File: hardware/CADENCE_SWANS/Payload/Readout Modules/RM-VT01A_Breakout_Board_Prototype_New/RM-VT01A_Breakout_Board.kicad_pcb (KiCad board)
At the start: 4 copper layers, 30.3 x 30.3 mm, 8 parts, among them J1 DE9_Pins

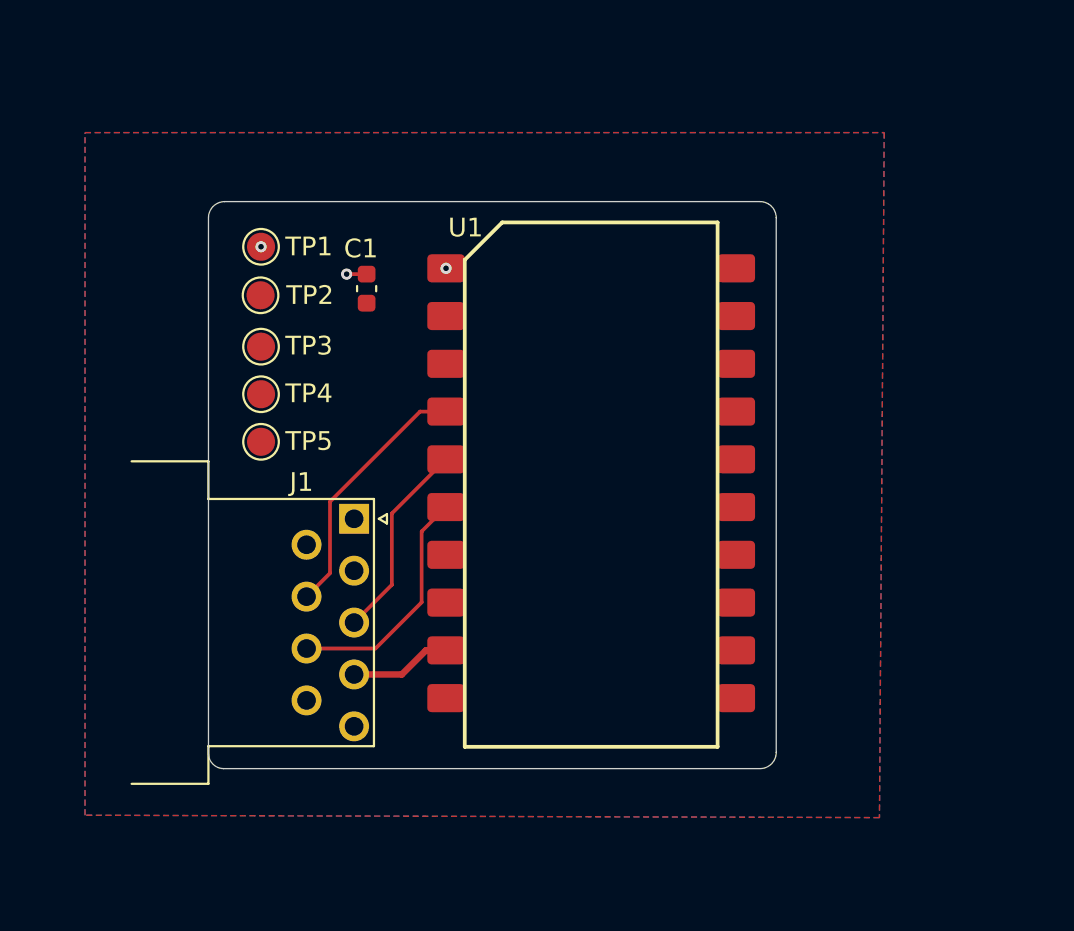
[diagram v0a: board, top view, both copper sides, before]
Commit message: Mounting Holes Included
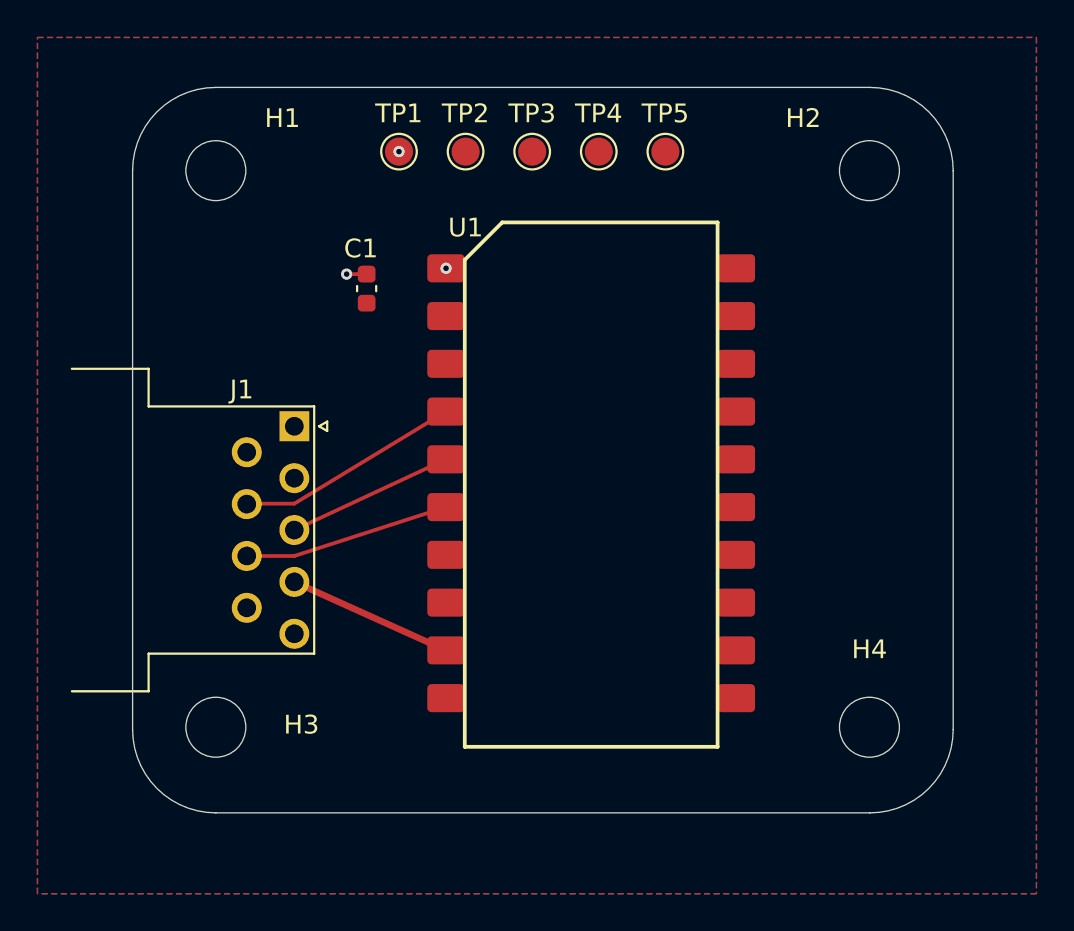
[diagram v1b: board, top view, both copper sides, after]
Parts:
- added H1: MountingHole, MountingHole:MountingHole_3.2mm_M3, F.Cu at (121.3, 68.1)
- added H2: MountingHole, MountingHole:MountingHole_3.2mm_M3, F.Cu at (156.2, 68.1)
- added H3: MountingHole, MountingHole:MountingHole_3.2mm_M3, F.Cu at (121.3, 97.8)
- added H4: MountingHole, MountingHole:MountingHole_3.2mm_M3, F.Cu at (156.2, 97.8)
- moved TP5 26.6 mm to (145.3, 67.1)
- moved TP4 22.2 mm to (141.7, 67.1)
- moved TP3 17.8 mm to (138.2, 67.1)
- moved TP2 13.4 mm to (134.6, 67.1)
- moved TP1 8.95 mm to (131.1, 67.1)
- moved J1 5.88 mm to (125.5, 81.7)
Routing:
- net CONN_COAXIAL: track 5.44 -> 8.89 mm
- net CTRL_EN: track 10.7 -> 8.94 mm
- net CTRL_R2: track 13.8 -> 12.0 mm
- net CTRL_R1: track 12.8 -> 11.0 mm
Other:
- board size 30.3 x 30.3 mm -> 43.8 x 38.7 mm

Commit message: Preliminary Update Payload
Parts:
- J1: footprint Connector_Dsub:DSUB-9_Pins_Horizontal_P2.77x2.54mm_EdgePinOffset9.40mm -> Imports:NORCOMP_380-009-213L001
- moved J1 2.47 mm to (124.4, 84.0), turned to 90 degrees
- renumbered TP4 to EN, TP2 to GND, TP5 to R1, TP3 to R2, TP1 to VDD
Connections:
- EN pad 1: unconnected-(TP4-Pad1) -> CTRL_EN
- R1 pad 1: unconnected-(TP5-Pad1) -> CTRL_R1
- R2 pad 1: unconnected-(TP3-Pad1) -> CTRL_R2
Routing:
- net CTRL_EN: track 8.94 -> 54.3 mm
- net CTRL_R1: track 11.0 -> 33.0 mm
- net CTRL_R2: track 12.0 -> 25.4 mm
- net CONN_COAXIAL: track 8.89 -> 15.8 mm
- net VDD: track 1.07 -> 4.59 mm, vias 3 -> 2
- net GND: vias 0 -> 3
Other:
- board text added: "Payload Instrument Board"
- board text removed: "Instrument Board"

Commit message: Revised Instrument Boards
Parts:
- removed the EN at (141.7, 67.1)
- removed the GND at (134.6, 67.1)
- removed the VDD at (131.1, 67.1)
- added EN: TestPoint, TestPoint:TestPoint_Loop_D2.60mm_Drill1.6mm_Beaded, F.Cu at (144.0, 66.3)
- added G***: LOGO, LOGO, B.Cu at (138.6, 92.5)
- added GND: TestPoint, TestPoint:TestPoint_Loop_D2.60mm_Drill1.6mm_Beaded, F.Cu at (134.6, 66.3)
- added VDD: TestPoint, TestPoint:TestPoint_Loop_D2.60mm_Drill1.6mm_Beaded, F.Cu at (129.9, 66.3)
- H1, H2, H3, H4: footprint MountingHole:MountingHole_3.2mm_M3 -> MountingHole:MountingHole_3.2mm_M3_ISO14580_Pad
- J1: footprint Imports:NORCOMP_380-009-213L001 -> Imports:CONN_381-009_NRC
- R1, R2: footprint TestPoint:TestPoint_Pad_D1.5mm -> TestPoint:TestPoint_Loop_D2.60mm_Drill1.6mm_Beaded
- moved J1 6.69 mm to (117.7, 83.8)
- moved R1 3.51 mm to (148.7, 66.3)
- moved R2 1.37 mm to (139.3, 66.3)
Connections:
- J1 pad 1: VDD -> CTRL_R2
- J1 pad 4: CONN_COAXIAL -> CTRL_R1
- J1 pad 5: GND -> CONN_COAXIAL
- J1 pad 6: unconnected-(J1-Pad6) -> VDD
- J1 pad 7: CTRL_R2 -> unconnected-(J1-Pad7)
- J1 pad 8: CTRL_R1 -> unconnected-(J1-Pad8)
- J1 pad 9: unconnected-(J1-Pad9) -> GND
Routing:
- net CTRL_EN: track 54.3 -> 27.9 mm
- net CONN_COAXIAL: track 15.8 -> 9.91 mm
- net CTRL_R2: track 25.4 -> 23.4 mm
- net VDD: track 4.59 -> 5.52 mm, vias 2 -> 1
- net GND: vias 3 -> 13
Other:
- board text added: "0.3493mm 50Ω"
- board text added: "Angelo Duenas Pragun Bethapudi"

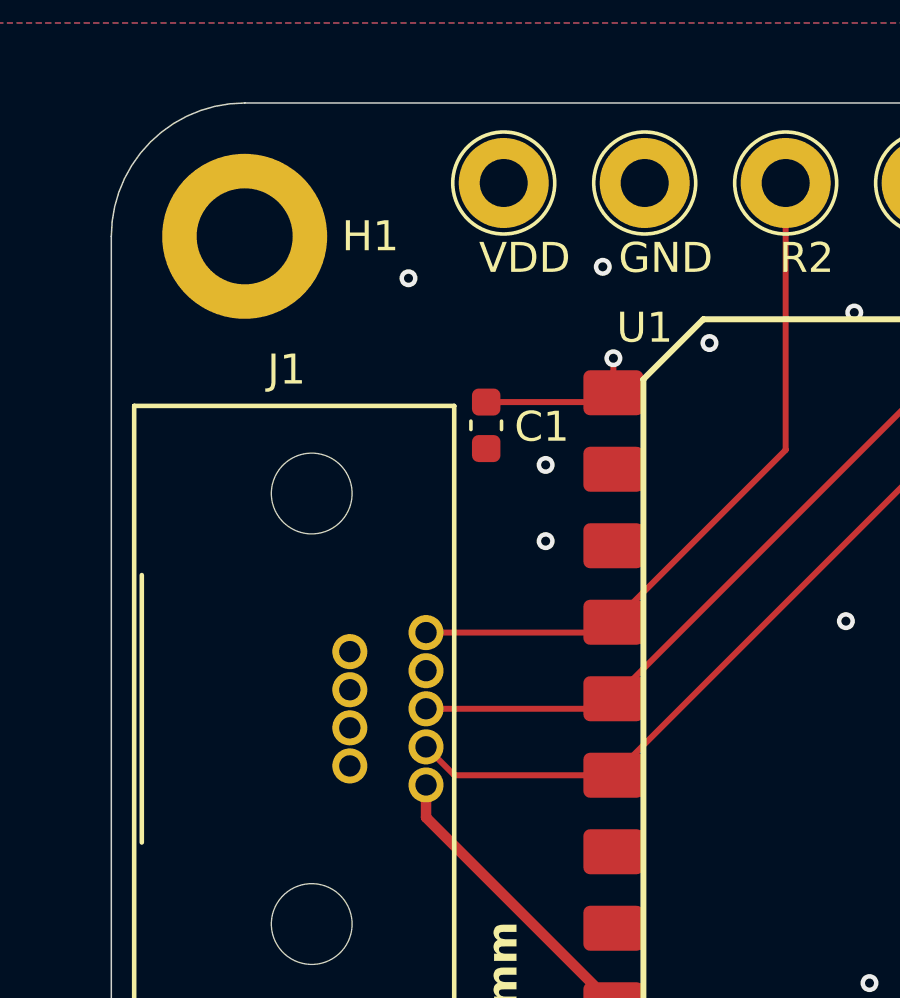
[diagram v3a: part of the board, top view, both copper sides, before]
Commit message: Updated Payload Instrument Boards
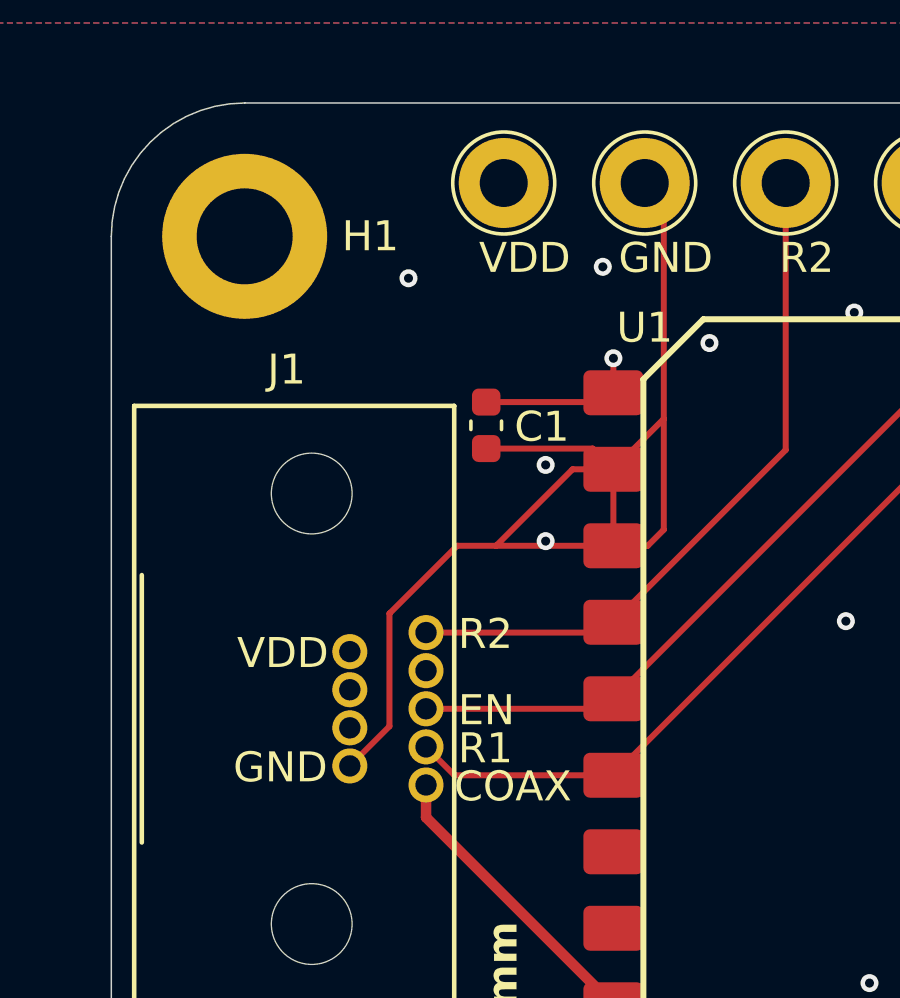
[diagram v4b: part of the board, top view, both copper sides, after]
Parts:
- added G***: LOGO, LOGO, B.Cu at (131.8, 94.6)
- moved G*** 8.00 mm to (146.6, 92.6)
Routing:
- net GND: track 0.00 -> 42.2 mm
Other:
- board text added: "COAX"
- board text added: "EN"
- board text added: "GND"
- board text added: "R1"
- board text added: "R2"
- board text added: "VDD"

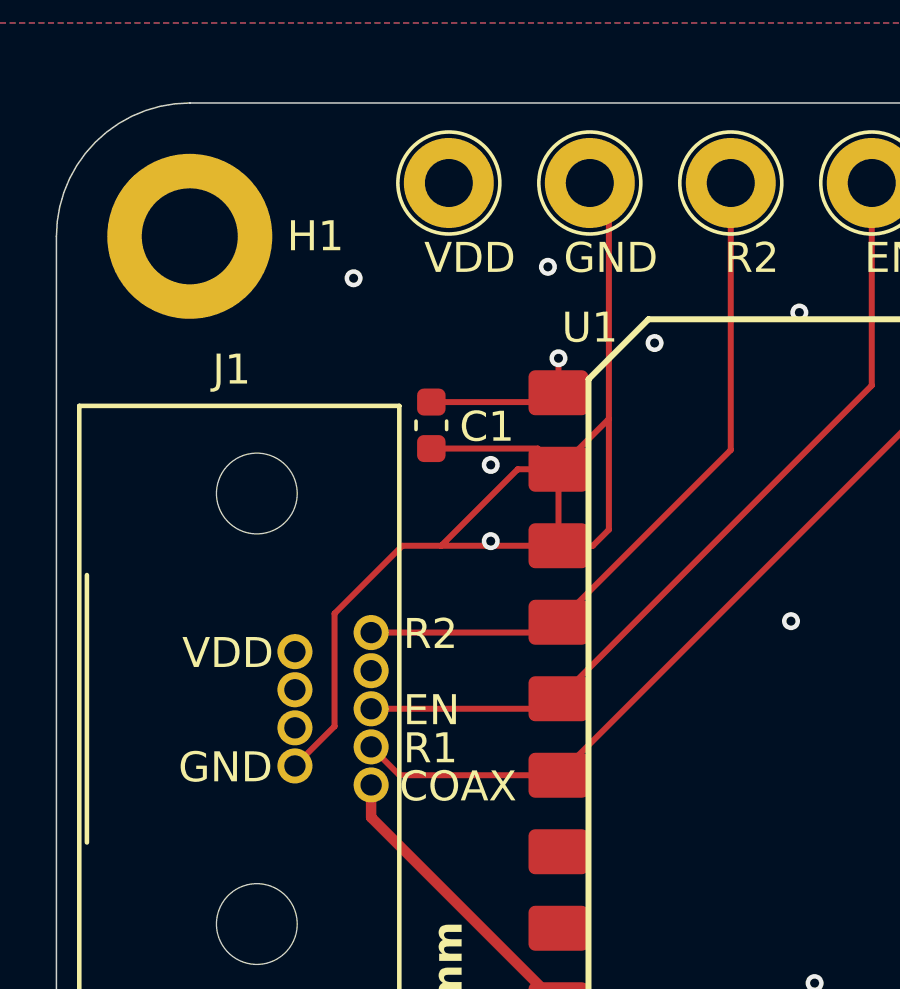
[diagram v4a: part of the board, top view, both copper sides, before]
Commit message: GND to Via Change
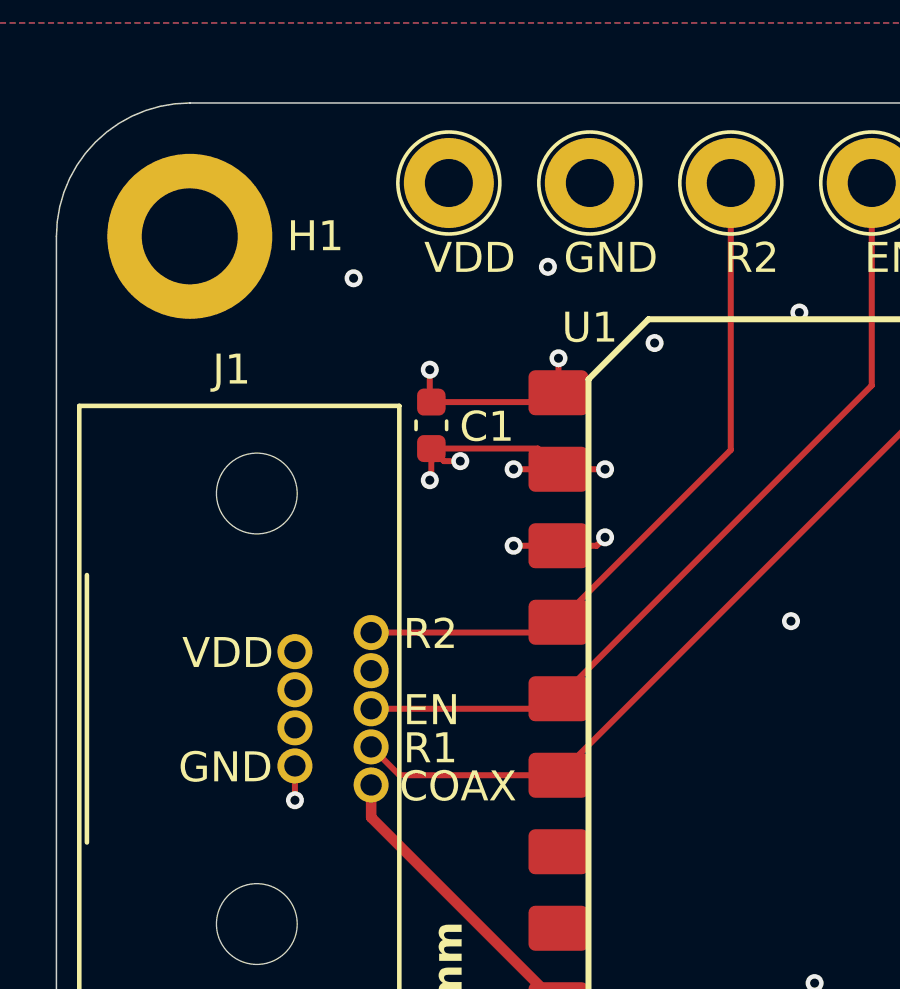
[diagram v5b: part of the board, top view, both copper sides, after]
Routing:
- net GND: track 42.2 -> 14.1 mm, vias 13 -> 18
- net VDD: track 5.52 -> 6.62 mm, vias 1 -> 2
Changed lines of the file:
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@@
-	)
-	(segment
-		(start 126.111 80.645)
-		(end 128.37 78.386)
-		(width 0.2)
-		(layer "F.Cu")
-		(net 2)
-	)
-	(segment
-		(start 134.62 66.294)
-		(end 135.255 66.929)
-		(width 0.2)
-		(layer "F.Cu")
-		(net 2)
 	)
 	(segment
@@
 	)
 	(segment
-		(start 135.255 74.1566)
+		(start 129.7556 75.565)
+		(end 129.3368 75.1462)
+		(width 0.2)
+		(layer "F.Cu")
+		(net 2)
+	)
+	(segment
+		(start 129.3368 76.1492)
+		(end 129.286 76.2)
+		(width 0.2)
+		(layer "F.Cu")
+		(net 2)
+	)
+	(segment
+		(start 132.08 78.386)
+		(end 133.5756 78.386)
+		(width 0.2)
+		(layer "F.Cu")
+		(net 2)
+	)
+	(segment
+		(start 135.128 78.105)
+		(end 134.847 78.386)
+		(width 0.2)
+		(layer "F.Cu")
+		(net 2)
+	)
+	(segment
+		(start 135.128 75.836)
 		(end 133.5756 75.836)
 		(width 0.2)
@@
 	)
 	(segment
-		(start 128.37 78.386)
-		(end 129.667 78.386)
-		(width 0.2)
-		(layer "F.Cu")
-		(net 2)
-	)
-	(segment
-		(start 133.5756 78.386)
-		(end 133.5756 75.836)
-		(width 0.2)
-		(layer "F.Cu")
-		(net 2)
-	)
-	(segment
-		(start 132.217 75.836)
-		(end 129.667 78.386)
-		(width 0.2)
-		(layer "F.Cu")
-		(net 2)
-	)
-	(segment
-		(start 129.667 78.386)
-		(end 133.5756 78.386)
-		(width 0.2)
-		(layer "F.Cu")
-		(net 2)
-	)
-	(segment
-		(start 126.111 84.4042)
-		(end 126.111 80.645)
-		(width 0.2)
-		(layer "F.Cu")
-		(net 2)
-	)
-	(segment
-		(start 135.255 74.1566)
-		(end 135.255 77.851)
+		(start 124.7902 86.868)
+		(end 124.7902 85.725)
 		(width 0.2)
 		(layer "F.Cu")
@@
 	)
 	(segment
-		(start 124.7902 85.725)
-		(end 126.111 84.4042)
-		(width 0.2)
-		(layer "F.Cu")
-		(net 2)
-	)
-	(segment
-		(start 133.5756 75.836)
-		(end 132.217 75.836)
-		(width 0.2)
-		(layer "F.Cu")
-		(net 2)
-	)
-	(segment
-		(start 135.255 66.929)
-		(end 135.255 74.1566)
-		(width 0.2)
-		(layer "F.Cu")
-		(net 2)
-	)
-	(segment
-		(start 135.255 77.851)
-		(end 134.72 78.386)
-		(width 0.2)
-		(layer "F.Cu")
-		(net 2)
-	)
-	(segment
-		(start 134.72 78.386)
+		(start 130.302 75.565)
+		(end 129.7556 75.565)
+		(width 0.2)
+		(layer "F.Cu")
+		(net 2)
+	)
+	(segment
+		(start 129.3368 75.1462)
+		(end 129.3368 76.1492)
+		(width 0.2)
+		(layer "F.Cu")
+		(net 2)
+	)
+	(segment
+		(start 132.08 75.836)
+		(end 133.5756 75.836)
+		(width 0.2)
+		(layer "F.Cu")
+		(net 2)
+	)
+	(segment
+		(start 134.847 78.386)
 		(end 133.5756 78.386)
 		(width 0.2)
@@
 	)
 	(via
+		(at 135.128 78.105)
+		(size 0.6)
+		(drill 0.3)
+		(layers "F.Cu" "B.Cu")
+		(free yes)
+		(net 2)
+	)
+	(via
 		(at 128.524 98.298)
 		(size 0.6)
@@
 	)
 	(via
+		(at 124.7902 86.868)
+		(size 0.6)
+		(drill 0.3)
+		(layers "F.Cu" "B.Cu")
+		(free yes)
+		(net 2)
+	)
+	(via
 		(at 133.223 69.088)
 		(size 0.6)
@@
 	)
 	(via
-		(at 131.318 78.232)
+		(at 132.08 78.386)
 		(size 0.6)
 		(drill 0.3)
@@
 	)
 	(via
-		(at 131.318 75.692)
+		(at 130.302 75.565)
+		(size 0.6)
+		(drill 0.3)
+		(layers "F.Cu" "B.Cu")
+		(free yes)
+		(net 2)
+	)
+	(via
+		(at 132.08 75.836)
 		(size 0.6)
 		(drill 0.3)
@@
 	)
 	(via
+		(at 129.286 76.2)
+		(size 0.6)
+		(drill 0.3)
+		(layers "F.Cu" "B.Cu")
+		(free yes)
+		(net 2)
+	)
+	(via
 		(at 136.779 71.628)
 		(size 0.6)
@@
 	)
 	(via
+		(at 135.128 75.836)
+		(size 0.6)
+		(drill 0.3)
+		(layers "F.Cu" "B.Cu")
+		(free yes)
+		(net 2)
+	)
+	(via
 		(at 142.113 92.964)
 		(size 0.6)
@@
 		(free yes)
 		(net 2)
+	)
+	(segment
+		(start 129.286 73.5454)
+		(end 129.3368 73.5962)
+		(width 0.2)
+		(layer "F.Cu")
+		(net 3)
 	)
 	(segment
@@
 	)
 	(segment
+		(start 129.286 72.517)
+		(end 129.286 73.5454)
+		(width 0.2)
+		(layer "F.Cu")
+		(net 3)
+	)
+	(segment
 		(start 133.5756 72.136)
 		(end 133.5756 73.286)
@@
 		(net 3)
 	)
+	(via
+		(at 129.286 72.517)
+		(size 0.6)
+		(drill 0.3)
+		(layers "F.Cu" "B.Cu")
+		(net 3)
+	)

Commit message: Payload Instrument Board Logo Adjustment
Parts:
- removed the G*** at (146.6, 92.6)
- removed the G*** at (131.8, 94.6)
- added G***: LOGO, LOGO, B.Cu at (144.1, 93.6)
- added G***: LOGO, LOGO, B.Cu at (133.2, 94.0)

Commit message: production files and removed one Vdd trace
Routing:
- net VDD: track 6.62 -> 5.47 mm, vias 2 -> 1
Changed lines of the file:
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@@
 			(psa4output no)
 			(plot_black_and_white yes)
+			(plotinvisibletext no)
 			(sketchpadsonfab no)
 			(plotpadnumbers no)
@@
 			"L6ss3F7Bp8Bkc2Ie46QWFs23eeCJd+C2inkVlDLNfgb+295TUZR7gEB8k7d2A5gWeq/4rqprdPVs"
 			"Y2PjrLVq4TYgTDJTipL3dwihsx64idGLfzrwIygY7yz5PYDfUmNwLv7vBqz1RowLhN8J4MI95brt"
-			"u+gYjgN/FD/FYs0V/GP4KRb5DM4rHH8/mLY4ed0p/D+urvIC1vkKVgAAAABJRU5ErkJggg=="
+			"u+gYjgN/FD/FYs0V/GP4KRb5DM4rHH8/mLY4ed0p/D+urvIC1vkKVgAAAABJRU5ErkJgggAAAAAA"
+			"AAAAAAAAAAAAAAAAAAAAAAAAAAAAAAAAAAAAAAAAAAAAAAAAAAAAAAAAAAAAAAAAAAAAAAAAAAAA"
+			"AAAAAAAAAAAAAAAAAAAAAAAAAAAAAAAAAAAAAAAAAAAAAAAAAAAAAAAAAAAAAAAAAAAAAAAAAAAA"
+			"AAAAAAAAAAAAAAAAAAAAAAAAAAAAAAAAAAAAAAAAAAAAAAAAAAAAAAAAAAAAAAAAAAAAAAAAAAAA"
+			"AAAAAAAAAAAAAAAAAAAAAAAAAAAAAAAAAAAAAAAAAAAAAAAAAAAAAAAAAAAAAAAAAAAAAAAAAAAA"
+			"AAAAAAAAAAAAAAAAAAAAAAAAAAAAAAAAAAAAAAAAAAAAAAAAAAAAAAAAAAAAAAAAAAAAAAAAAAAA"
+			"AAAAAAAAAAAAAAAAAAAAAAAAAAAAAAAAAAAAAAAAAAAAAAAAAAAAAAAAAAAAAAAAAAAAAAAAAAAA"
+			"AAAAAAAAAAAAAAAAAAAAAAAAAAAAAAAAAAAAAAAAAAAAAAAAAAAAAAAAAAAAAAAAAAAAAAAAAAAA"
+			"AAAAAAAAAAAAAAAAAAAAAAAAAAAAAAAAAAAAAAAAAAAAAAAAAAAAAAAAAAAAAAAAAAAAAAAAAAAA"
+			"AAAAAAAAAAAAAAAAAAAAAAAAAAAAAAAAAAAAAAAAAAAAAAAAAAAAAAAAAAAAAAAAAAAAAAAAAAAA"
+			"AAAAAAAAAAAAAAAAAAAAAAAAAAAAAAAAAAAAAAAAAAAAAAAAAAAAAAAAAAAAAAAAAAAAAAAAAAAA"
+			"AAAAAAAAAAAAAAAAAAAAAAAAAAAAAAAAAAAAAAAAAAAAAAAAAAAAAAAAAAAAAAAAAAAAAAAAAAAA"
+			"AAAAAAAAAAAAAAAAAAAAAAAAAAAAAAAAAAAAAAAAAAAAAAAAAAAAAAAAAAAAAAAAAAAAAAAAAAAA"
+			"AAAAAAAAAAAAAAAAAAAAAAAAAAAAAAAAAAAAAAAAAAAAAAAAAAAAAAAAAAAAAAAAAAAAAAAAAAAA"
+			"AAAAAAAAAAAAAAAAAAAAAAAAAAAAAAAAAAAAAAAAAAAAAAAAAAAAAAAAAAAAAAAAAAAAAAAAAAAA"
+			"AAAAAAAAAAAAAAAAAAAAAAAAAAAAAAAAAAAAAAAAAAAAAAAAAAAAAAAAAAAAAAAAAAAAAAAAAAAA"
+			"AAAAAAAAAAAAAAAAAAAAAAAAAAAAAAAAAAAAAAAAAAAAAAAAAAAAAAAAAAAAAAAAAAAAAAAAAAAA"
+			"AAAAAAAAAAAAAAAAAAAAAAAAAAAAAAAAAAAAAAAAAAAAAAAAAAAAAAAAAAAAAAAAAAAAAAAAAAAA"
+			"AAAAAAAAAAAAAAAAAAAAAAAAAAAAAAAAAAAAAAAAAAAAAAAAAAAAAAAAAAAAAAAAAAAAAA=="
 		)
 	)
@@
 	)
 	(segment
-		(start 133.5756 72.136)
-		(end 133.5756 73.286)
-		(width 0.2)
-		(layer "F.Cu")
-		(net 3)
-	)
-	(segment
 		(start 129.3368 73.5962)
 		(end 133.2654 73.5962)
@@
 		(size 0.6)
 		(drill 0.3)
-		(layers "F.Cu" "B.Cu")
-		(net 3)
-	)
-	(via
-		(at 133.5756 72.136)
-		(size 0.6)
-		(drill 0.3)
